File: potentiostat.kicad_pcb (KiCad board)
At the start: 2 copper layers, 38.8 x 55 mm, 30 parts, among them J1 Conn_01x01_Socket, J2 Conn_01x01_Socket, SW1 SW_Push, SW2 SW_Push, U1 ESP32-WROOM-32, U2 AD9833xRM, U3 TLV2372ID, U4 AMS1117-3.3, Y2 25MHz

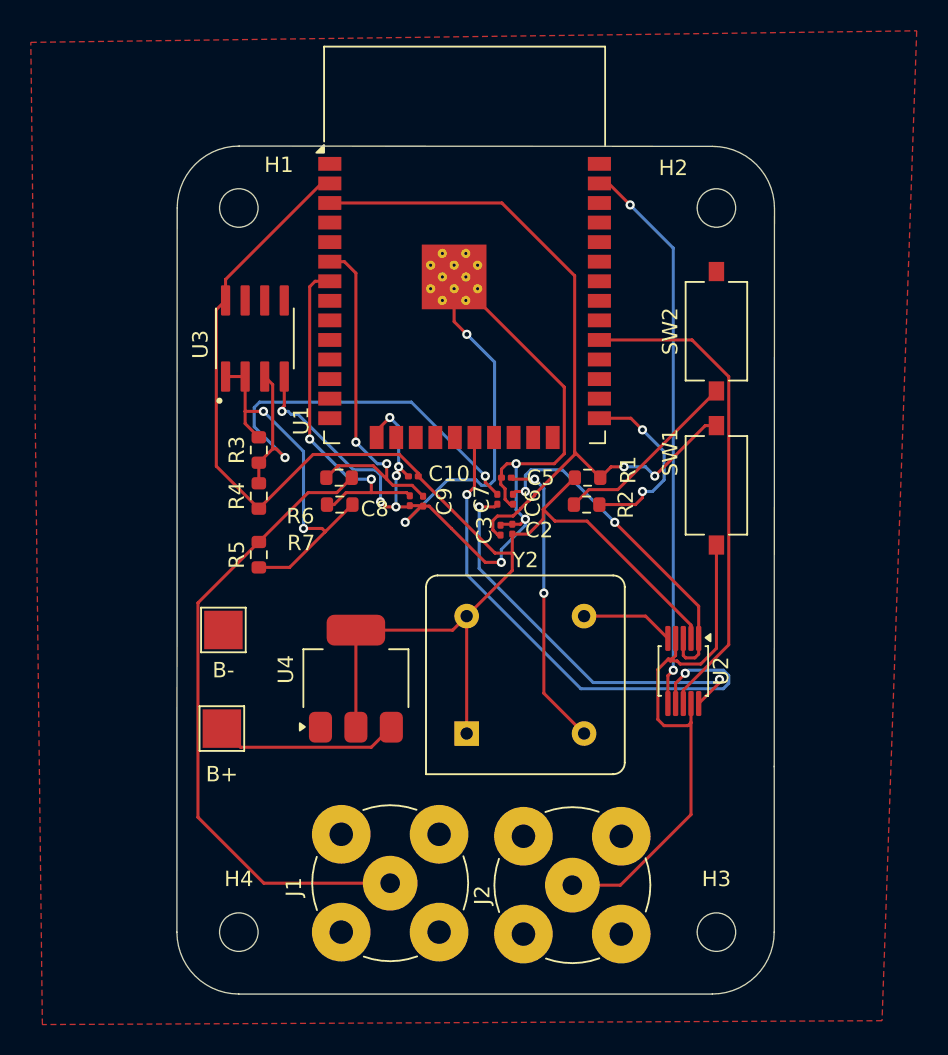
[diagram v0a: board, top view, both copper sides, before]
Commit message: dip switch added
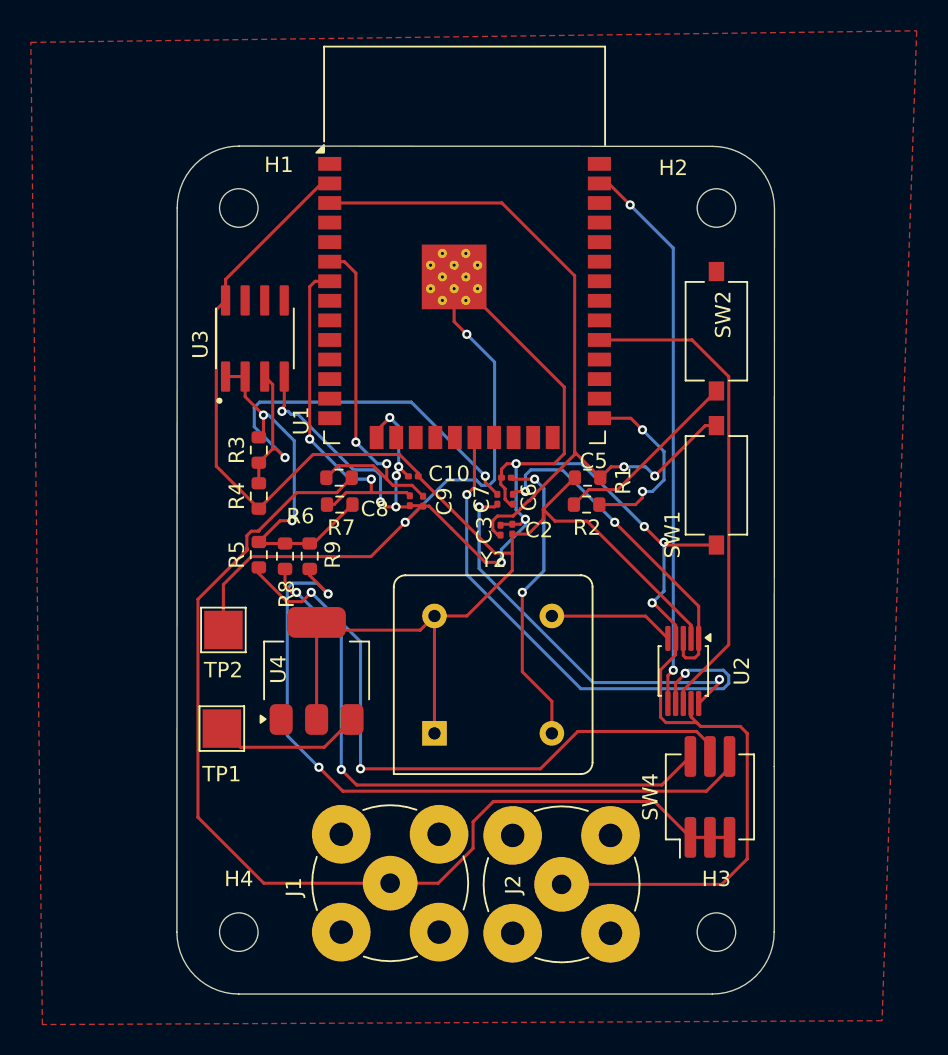
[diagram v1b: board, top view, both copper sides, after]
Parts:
- added G***: LOGO, assets:watchdog, B.Cu at (140.1, 88.8)
- added R8: 10K, Resistor_SMD:R_0603_1608Metric, F.Cu at (116.0, 100.6)
- added R9: 10K, Resistor_SMD:R_0603_1608Metric, F.Cu at (117.6, 100.6)
- added SW4: SW_DIP_x03, Button_Switch_SMD:SW_DIP_SPSTx03_Slide_KingTek_DSHP03TJ_W5.25mm_P1.27mm_JPin, F.Cu at (143.6, 116.2)
- moved U4 2.60 mm to (118.0, 108.0)
- moved Y2 2.09 mm to (125.7, 112.1)
- moved J2 0.70 mm to (133.9, 121.9)
- renumbered B+ to TP1, B- to TP2
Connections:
- R5 pad 1: BUF_OUT -> Net-(R5-Pad1)
- R5 pad 2: Net-(J1-Pin_1) -> BUF_OUT
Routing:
- net Net-(R9-Pad1): track 0.00 -> 46.3 mm, vias 0 -> 2
- net Net-(R5-Pad1): track 0.00 -> 42.4 mm, vias 0 -> 2
- net Net-(R8-Pad1): track 0.00 -> 38.6 mm, vias 0 -> 2
- net GND: track 119.7 -> 156.9 mm, vias 11 -> 14
- net Net-(J1-Pin_1): track 41.5 -> 68.4 mm
- net +3.3V: track 93.9 -> 96.6 mm
- net Net-(U4-VI): track 12.0 -> 9.70 mm
- net Net-(U2-MCLK): track 6.04 -> 8.13 mm
- net BUF_OUT: track 24.7 -> 23.4 mm
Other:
- board text added: "IMPEDANCE MEASUREMENT TOOL"

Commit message: debugging pins
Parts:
- added J3: Conn_01x03_Pin, Connector_PinHeader_2.54mm:PinHeader_1x03_P2.54mm_Horizontal, F.Cu at (112.8, 119.9)
- moved B+ 1.81 mm to (112.0, 110.0)
- renumbered TP1 to B+, TP2 to B-
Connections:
- U1 pad 34: unconnected-(U1-RXD0/IO3-Pad34) -> RX
- U1 pad 35: unconnected-(U1-TXD0/IO1-Pad35) -> TX
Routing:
- net RX: track 0.00 -> 63.3 mm, vias 0 -> 4
- net TX: track 0.00 -> 55.2 mm, vias 0 -> 2
- net GND: track 156.9 -> 174.8 mm, vias 14 -> 16
- net Net-(U4-VI): track 9.70 -> 11.6 mm
- net Net-(J1-Pin_1): track 68.4 -> 69.9 mm
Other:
- board text added: "Gnd"
- board text added: "Rx"
- board text added: "Tx"
